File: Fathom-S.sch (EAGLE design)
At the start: 112 parts, among them IC1 LMH6643, IC2 LMH6643, IC3 ST490AB, IC4 ST490AB, IC5 FT230XS, Q1 BC817-40W, U1 MC7812, U2 MC7805, U4 INA139, U5 MC7805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

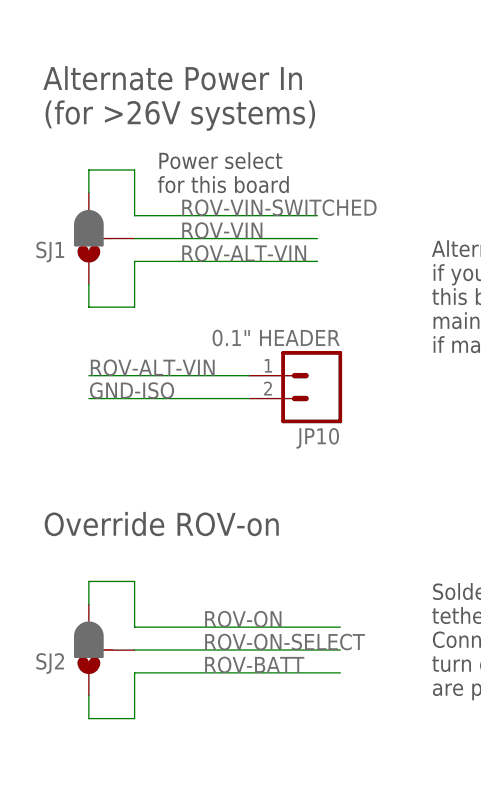
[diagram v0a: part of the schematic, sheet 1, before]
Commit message: Changed jumpers from solder to headers. This rev4 and the beta boards will be ordered from this commit.
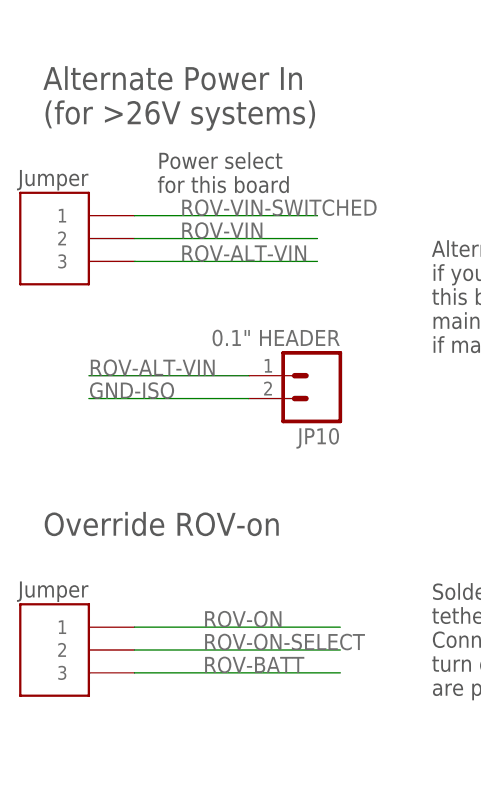
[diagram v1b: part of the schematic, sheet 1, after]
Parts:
- removed SJ1, SJ2: JUMPER-PAD-3-2OF3_NC_BY_PASTE, SparkFun-Passives:JUMPER-PAD-3-2OF3_NC_BY_PASTE
- removed SJ4: JUMPER-PAD-2-NC_BY_PASTE, SparkFun-Passives:JUMPER-PAD-2-NC_BY_PASTE
- added U$13, U$14: HEADER-33MM, BlueRobotics-Main:HEADER-33MM
- added U$16: HEADER-22MM, BlueRobotics-Main:HEADER-22MM
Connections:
- net N$7: now also U$16.1; no longer SJ4.2
- net ROV-ALT-VIN: now also U$14.3; no longer SJ1.1
- net ROV-BATT: now also U$13.3; no longer SJ2.1
- net ROV-ON: now also U$13.1; no longer SJ2.3
- net ROV-ON-SELECT: now also U$13.2; no longer SJ2.2
- net ROV-VIN: now also U$14.2; no longer SJ1.2
- net ROV-VIN-SWITCHED: now also U$14.1; no longer SJ1.3
- net RTS: now also U$16.2; no longer SJ4.1
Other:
- note added: "Jumper"

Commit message: Massive revision to simplify and make easier to use. Added DroneCode connectors, removed excessive stuff, and removed power switching.
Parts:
- removed C25: 0.1uF, SparkFun-Passives:CAP0603-CAP
- removed D2: Schottky, SparkFun-DiscreteSemi:DIODESOD
- removed JP10, JP4, JP9: 0.1" HEADER, SparkFun-Connectors:M02PTH
- removed R15, R16: NP, resistor:R-US_R1210
- removed R26, R28, R29, R31: 0, SparkFun:RESISTOR1206
- removed R34: 0.001 1% 3W, SparkFun-Resistors:RESISTOR2512
- removed R36: 18K 1%, SparkFun-Resistors:33KOHM1/10W1%(0603)
- removed R37: 2.2K 1%, SparkFun-Resistors:33KOHM1/10W1%(0603)
- removed R44: 68K 1%, SparkFun-Resistors:33KOHM1/10W1%(0603)
- removed R45: 1K, SparkFun-Resistors:33KOHM1/10W1%(0603)
- removed U$14: HEADER-33MM, BlueRobotics-Main:HEADER-33MM
- removed U4: INA139, SparkFun-AnalogIC:INA139
- added C28, C29: 1uF, SparkFun-Passives:CAP0603-CAP
- added JP5: M02PTH, SparkFun-Connectors:M02PTH
- added U$15: VREG-MIC5365, BlueRobotics-Main:VREG-MIC5365
- C10: value 10uF 16V -> 47uF 10V; device SparkFun-Passives:CAP_POL1206 -> SparkFun-Passives:CAP_POL3528
- C24: device SparkFun-Passives:CAP0603-CAP -> SparkFun:CAP0603-CAP
- JP1: value PJRAN1X1U04X -> (none); device BlueRobotics-Main:RCA -> SparkFun-Connectors:M04PTH
- U$10, U$12: value HEADER-2 -> M023.5MM; device BR-Eagle-Library:HEADER-2 -> SparkFun-Connectors:M023.5MM
- U$11: value HEADER-2 -> JST-GH-6TOP-ENTRY; device BR-Eagle-Library:HEADER-2 -> BlueRobotics-JST-GH:JST-GH-6TOP-ENTRY
- U$3: value Si4459ADY -> DF13-6P-1.25V; device SparkFun-DiscreteSemi:MOSFET-PCHANNEL-SOIC8SOIC8 -> con-hirose-df13:DF13-6P-1.25V
- U$6: value Si4459ADY -> AO4407A
- U$8: value TETHER-HEADERSERIAL -> TXS0102DCUR; device BR-Eagle-Library:TETHER-HEADERSERIAL -> BlueRobotics-Main:TXS0102
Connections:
- removed net I_SENSE: D2.A, R45.2, U$8.I_SENSE
- removed net N$23: IC3G$1.Y, R28.1
- removed net N$24: IC4G$1.Y, R31.1
- removed net N$25: IC4G$1.Z, R29.1
- removed net N$26: IC3G$1.Z, R26.1
- removed net N$33: C25.1, R44.1, R45.1, U4.OUT
- removed net ROV-ALT-VIN: JP10.1, U$14.3
- removed net ROV-VIN-PRESENSE: R34.2, U$3.D@1, U$3.D@2, U$3.D@3, U$3.D@4, U$6.D@1, U$6.D@2, U$6.D@3, U$6.D@4, U4.VIN+
- removed net ROV-VIN-SWITCHED: R34.1, R36.2, U$11.1, U$14.1, U4.VIN-
- removed net V_SENSE: R36.1, R37.2, U$8.V_SENSE
- new net 3.3V-ISO: C24.1, C29.1, U$15.VOUT, U$8.OE, U$8.VCCA
- new net RX-3.3V: JP1.2, U$11.3, U$3.3, U$8.A2
- new net TX-3.3V: JP1.1, U$11.2, U$3.2, U$8.A1
- net 12V-ISO: no longer U$8.12V
- net CAMERA: no longer JP1.PIN, U$8.VIDEO
- net GND: no longer JP4.2, JP9.2
- net GND-ISO: now also C28.2, C29.2, JP1.4, JP5.1, U$11.6, U$15.GND, U$3.6; no longer C25.2, JP1.SHELL, JP10.2, R37.1, R44.2, U$11.2, U4.GND
- net N$28: no longer U$3.G
- net ROV-BATT: no longer U$3.S@1, U$3.S@2, U$3.S@3
- net ROV-RX: now also U$8.B2; no longer U$8.RX
- net ROV-TP2+: now also IC4G$1.Y; no longer R31.2
- net ROV-TP2-: now also IC4G$1.Z; no longer R29.2
- net ROV-TP3+: no longer R16.2
- net ROV-TP3-: no longer R16.1
- net ROV-TX: now also U$8.B1; no longer U$8.TX
- net ROV-VIN: now also JP5.2, U$6.D@1, U$6.D@2, U$6.D@3, U$6.D@4; no longer U$14.2, U$8.VBAT
- net TOP-TP2+: no longer R15.2
- net TOP-TP2-: no longer R15.1
- net TOP-TP3+: now also IC3G$1.Y; no longer R28.2
- net TOP-TP3-: now also IC3G$1.Z; no longer R26.2
- net TOP-VIN: no longer JP9.1
- net VCC: no longer JP4.1
- net VCC-ISO: now also C28.1, JP1.3, U$11.1, U$15.EN, U$15.VIN, U$3.1, U$8.VCCB; no longer C24.1, D2.C, U$8.5V, U4.V+
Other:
- note added: "5V-3.3V Level Shifting"
- note added: "DroneCode JST-GH Serial Port"
- note added: "PixHawk/APM DF13 Serial Port"
- note added: "Power Supply, VIN to 3.3V (ROV)"
- note added: "Serial Port (0.1" Header, DF13, JST-GH)"
- note added: "Switched Battery Power (May someday be used to switch on separate power board)"
- note added: "Switched Power Access"
- note removed: "12V output for cameras (unregulated if Vin < 13V) (1A w/ 12Vin) (150 mA w/ 24Vin)"
- note removed: "5V accessory power output for µC, etc. (400mA+ w/ USB power) (250mA w/ 12Vin) (100mA w/ 24Vin)"
- note removed: "Accessory 5V Power"
- note removed: "Accessory Vin Power"
- note removed: "Accessory power directly from alternate TOP-VIN"
- note removed: "Alternate Power In (for >26V systems)"
- note removed: "Alternate power input if you don't want to power this board from the main batteries. (Supply 12V if main battery if > 26V)"
- note removed: "Current Sense"
- note removed: "Power select for this board"
- note removed: "Ribbon cable provides single-cable connection to ROV controller"
- note removed: "Switched battery output for electronics and/or medium power applications (40A peak, 20A continuous)"
- note removed: "Termination resistors removed to minimize power losses. If required, use: Series resistors: 43 ohm 1/4 W Parallel resistor: 86.6 ohm, 1/2 W"
- note removed: "Tether Interface Header (for 2x6 ribbon cable)"
- note removed: "VIN for all regulators is up to 37V"
- note removed: "Voltage Sense"
- note removed: "~16 Hz Bandwidth Limit"

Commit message: Change 12V output capacitor size.
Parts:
- C13: value 10uF 25V -> 33uF 20V
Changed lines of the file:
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@@
 <grid distance="0.1" unitdist="inch" unit="inch" style="lines" multiple="1" display="no" altdistance="0.01" altunitdist="inch" altunit="inch"/>
 <layers>
-<layer number="1" name="Top" color="4" fill="1" visible="yes" active="no"/>
-<layer number="2" name="Route2" color="1" fill="3" visible="yes" active="no"/>
-<layer number="3" name="Route3" color="4" fill="3" visible="yes" active="no"/>
-<layer number="14" name="Route14" color="1" fill="6" visible="yes" active="no"/>
-<layer number="15" name="Route15" color="4" fill="6" visible="yes" active="no"/>
-<layer number="16" name="Bottom" color="1" fill="1" visible="yes" active="no"/>
-<layer number="17" name="Pads" color="2" fill="1" visible="yes" active="no"/>
-<layer number="18" name="Vias" color="2" fill="1" visible="yes" active="no"/>
-<layer number="19" name="Unrouted" color="6" fill="1" visible="yes" active="no"/>
-<layer number="20" name="Dimension" color="15" fill="1" visible="yes" active="no"/>
-<layer number="21" name="tPlace" color="3" fill="1" visible="yes" active="no"/>
-<layer number="22" name="bPlace" color="3" fill="1" visible="yes" active="no"/>
-<layer number="23" name="tOrigins" color="15" fill="1" visible="yes" active="no"/>
-<layer number="24" name="bOrigins" color="15" fill="1" visible="yes" active="no"/>
-<layer number="25" name="tNames" color="7" fill="1" visible="yes" active="no"/>
-<layer number="26" name="bNames" color="7" fill="1" visible="yes" active="no"/>
-<layer number="27" name="tValues" color="7" fill="1" visible="yes" active="no"/>
-<layer number="28" name="bValues" color="7" fill="1" visible="yes" active="no"/>
+<layer number="1" name="Top" color="4" fill="1" visible="no" active="no"/>
+<layer number="2" name="Route2" color="1" fill="3" visible="no" active="no"/>
+<layer number="3" name="Route3" color="4" fill="3" visible="no" active="no"/>
+<layer number="14" name="Route14" color="1" fill="6" visible="no" active="no"/>
+<layer number="15" name="Route15" color="4" fill="6" visible="no" active="no"/>
+<layer number="16" name="Bottom" color="1" fill="1" visible="no" active="no"/>
+<layer number="17" name="Pads" color="2" fill="1" visible="no" active="no"/>
+<layer number="18" name="Vias" color="2" fill="1" visible="no" active="no"/>
+<layer number="19" name="Unrouted" color="6" fill="1" visible="no" active="no"/>
+<layer number="20" name="Dimension" color="15" fill="1" visible="no" active="no"/>
+<layer number="21" name="tPlace" color="3" fill="1" visible="no" active="no"/>
+<layer number="22" name="bPlace" color="3" fill="1" visible="no" active="no"/>
+<layer number="23" name="tOrigins" color="15" fill="1" visible="no" active="no"/>
+<layer number="24" name="bOrigins" color="15" fill="1" visible="no" active="no"/>
+<layer number="25" name="tNames" color="7" fill="1" visible="no" active="no"/>
+<layer number="26" name="bNames" color="7" fill="1" visible="no" active="no"/>
+<layer number="27" name="tValues" color="7" fill="1" visible="no" active="no"/>
+<layer number="28" name="bValues" color="7" fill="1" visible="no" active="no"/>
 <layer number="29" name="tStop" color="7" fill="3" visible="no" active="no"/>
 <layer number="30" name="bStop" color="7" fill="6" visible="no" active="no"/>
@@
 <layer number="35" name="tGlue" color="7" fill="4" visible="no" active="no"/>
 <layer number="36" name="bGlue" color="7" fill="5" visible="no" active="no"/>
-<layer number="37" name="tTest" color="7" fill="1" visible="yes" active="no"/>
-<layer number="38" name="bTest" color="7" fill="1" visible="yes" active="no"/>
+<layer number="37" name="tTest" color="7" fill="1" visible="no" active="no"/>
+<layer number="38" name="bTest" color="7" fill="1" visible="no" active="no"/>
 <layer number="39" name="tKeepout" color="4" fill="11" visible="no" active="no"/>
 <layer number="40" name="bKeepout" color="1" fill="11" visible="no" active="no"/>
@@
 <layer number="44" name="Drills" color="7" fill="1" visible="no" active="no"/>
 <layer number="45" name="Holes" color="7" fill="1" visible="no" active="no"/>
-<layer number="46" name="Milling" color="3" fill="1" visible="yes" active="no"/>
-<layer number="47" name="Measures" color="7" fill="1" visible="yes" active="no"/>
-<layer number="48" name="Document" color="7" fill="1" visible="yes" active="no"/>
-<layer number="49" name="Reference" color="7" fill="1" visible="yes" active="no"/>
-<layer number="50" name="dxf" color="7" fill="1" visible="yes" active="no"/>
-<layer number="51" name="tDocu" color="3" fill="1" visible="yes" active="no"/>
-<layer number="52" name="bDocu" color="3" fill="1" visible="yes" active="no"/>
-<layer number="53" name="tGND_GNDA" color="7" fill="9" visible="yes" active="no"/>
-<layer number="54" name="bGND_GNDA" color="1" fill="9" visible="yes" active="no"/>
-<layer number="56" name="wert" color="7" fill="1" visible="yes" active="no"/>
-<layer number="57" name="tCAD" color="7" fill="1" visible="yes" active="no"/>
+<layer number="46" name="Milling" color="3" fill="1" visible="no" active="no"/>
+<layer number="47" name="Measures" color="7" fill="1" visible="no" active="no"/>
+<layer number="48" name="Document" color="7" fill="1" visible="no" active="no"/>
+<layer number="49" name="Reference" color="7" fill="1" visible="no" active="no"/>
+<layer number="50" name="dxf" color="7" fill="1" visible="no" active="no"/>
+<layer number="51" name="tDocu" color="3" fill="1" visible="no" active="no"/>
+<layer number="52" name="bDocu" color="3" fill="1" visible="no" active="no"/>
+<layer number="53" name="tGND_GNDA" color="7" fill="9" visible="no" active="no"/>
+<layer number="54" name="bGND_GNDA" color="1" fill="9" visible="no" active="no"/>
+<layer number="56" name="wert" color="7" fill="1" visible="no" active="no"/>
+<layer number="57" name="tCAD" color="7" fill="1" visible="no" active="no"/>
 <layer number="90" name="Modules" color="5" fill="1" visible="yes" active="yes"/>
 <layer number="91" name="Nets" color="2" fill="1" visible="yes" active="yes"/>
@@
 <part name="R25" library="SparkFun-Resistors" deviceset="33KOHM1/10W1%(0603)" device="" value="10K"/>
 <part name="D1" library="SparkFun-DiscreteSemi" deviceset="DIODE-ZENER" device="3.3V" value="16V"/>
-<part name="C13" library="SparkFun-Passives" deviceset="CAP_POL" device="6032" value="10uF 25V"/>
+<part name="C13" library="SparkFun-Passives" deviceset="CAP_POL" device="6032" value="33uF 20V"/>
 <part name="FRAME1" library="BlueRobotics-Main" deviceset="FRAME-BLUEROBOTICS" device="" value="Onboard Connectors &amp; Misc."/>
 <part name="FRAME2" library="BlueRobotics-Main" deviceset="FRAME-BLUEROBOTICS" device="" value="Video Amplifiers"/>
